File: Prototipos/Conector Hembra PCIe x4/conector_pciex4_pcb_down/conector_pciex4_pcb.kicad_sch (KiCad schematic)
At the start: 33 parts, among them J1 10018783-10211TLF

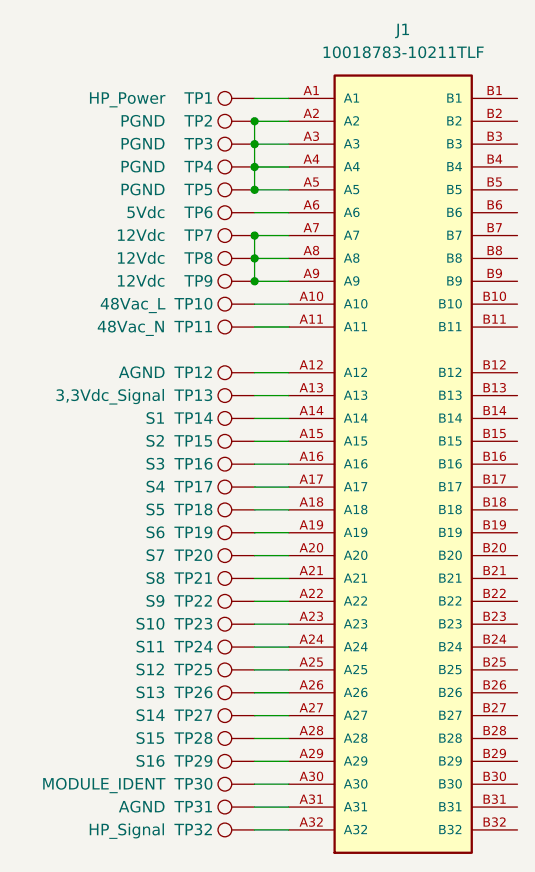
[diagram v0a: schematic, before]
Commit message: Agregado de otra configuración de pines
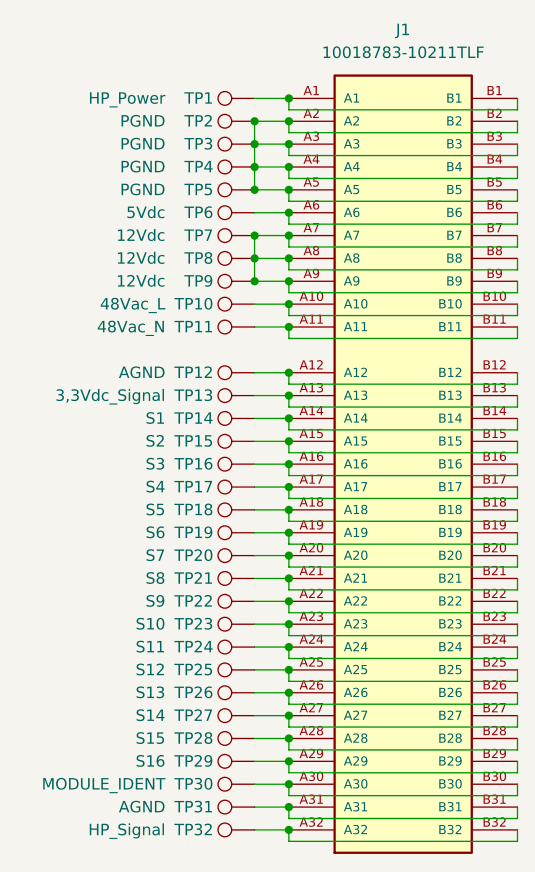
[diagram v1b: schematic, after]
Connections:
- net at J1.A20, TP20.1: now also J1.B20
- net at J1.A25, TP25.1: now also J1.B25
- net at J1.A32, TP32.1: now also J1.B32
- net at J1.A31, TP31.1: now also J1.B31
- net at J1.A26, TP26.1: now also J1.B26
- net at J1.A13, TP13.1: now also J1.B13
- net at J1.A12, TP12.1: now also J1.B12
- net at J1.A16, TP16.1: now also J1.B16
- net at J1.A29, TP29.1: now also J1.B29
- net at J1.A22, TP22.1: now also J1.B22
- net at J1.A2, J1.A3, J1.A4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: now also J1.B2, J1.B3, J1.B4, J1.B5
- net at J1.A28, TP28.1: now also J1.B28
- net at J1.A1, TP1.1: now also J1.B1
- net at J1.A15, TP15.1: now also J1.B15
- net at J1.A6, TP6.1: now also J1.B6
- net at J1.A17, TP17.1: now also J1.B17
- net at J1.A10, TP10.1: now also J1.B10
- net at J1.A21, TP21.1: now also J1.B21
- net at J1.A19, TP19.1: now also J1.B19
- net at J1.A7, J1.A8, J1.A9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: now also J1.B7, J1.B8, J1.B9
- net at J1.A11, TP11.1: now also J1.B11
- net at J1.A18, TP18.1: now also J1.B18
- net at J1.A14, TP14.1: now also J1.B14
- net at J1.A23, TP23.1: now also J1.B23
- net at J1.A24, TP24.1: now also J1.B24
- net at J1.A27, TP27.1: now also J1.B27
- net at J1.A30, TP30.1: now also J1.B30
